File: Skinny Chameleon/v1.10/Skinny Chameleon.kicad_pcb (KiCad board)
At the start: 2 copper layers, 225.4 x 91.9 mm, 206 parts, among them SW10 PG151101S11, SW11 PG151101S11, SW13 PG151101S11, SW14 PG151101S11, SW15 PG151101S11, SW16 PG151101S11, SW17 PG151101S11, SW18 PG151101S11, SW19 PG151101S11, SW2 PG151101S11, SW20 PG151101S11, SW21 PG151101S11, SW22 PG151101S11, SW23 PG151101S11, SW24 PG151101S11, SW25 PG151101S11, SW26 PG151101S11, SW27 PG151101S11, SW28 PG151101S11, SW29 PG151101S11, SW3 PG151101S11, SW30 PG151101S11, SW31 PG151101S11, SW32 PG151101S11, SW33 PG151101S11, SW34 PG151101S11, SW35 PG151101S11, SW36 PG151101S11, SW38 PG151101S11, SW39 PG151101S11, SW4 PG151101S11, SW40 PG151101S11, SW41 PG151101S11, SW42 PG151101S11, SW43 PG151101S11, SW44 PG151101S11, SW45 PG151101S11, SW46 PG151101S11, SW47 PG151101S11, SW5 PG151101S11, SW50 PG151101S11, SW51 PG151101S11, SW52 PG151101S11, SW53 PG151101S11, SW54 PG151101S11, SW55 PG151101S11, SW56 PG151101S11, SW57 PG151101S11, SW58 PG151101S11, SW59 PG151101S11, SW6 PG151101S11, SW61 PG151101S11, SW62 PG151101S11, SW63 PG151101S11, SW64 PG151101S11, SW65 PG151101S11, SW66 PG151101S11, SW67 YTSA010, SW68 YTSA010, SW7 PG151101S11, SW8 PG151101S11, SW9 PG151101S11, U1 SPX3819M5-L-3-3/TR, U2 W25Q32JVUUIQ, U3 RP2040, U4 SN74LV1T34DBV, U5 SRV05-4, Y1 TXM12M0004252LBCEO00T

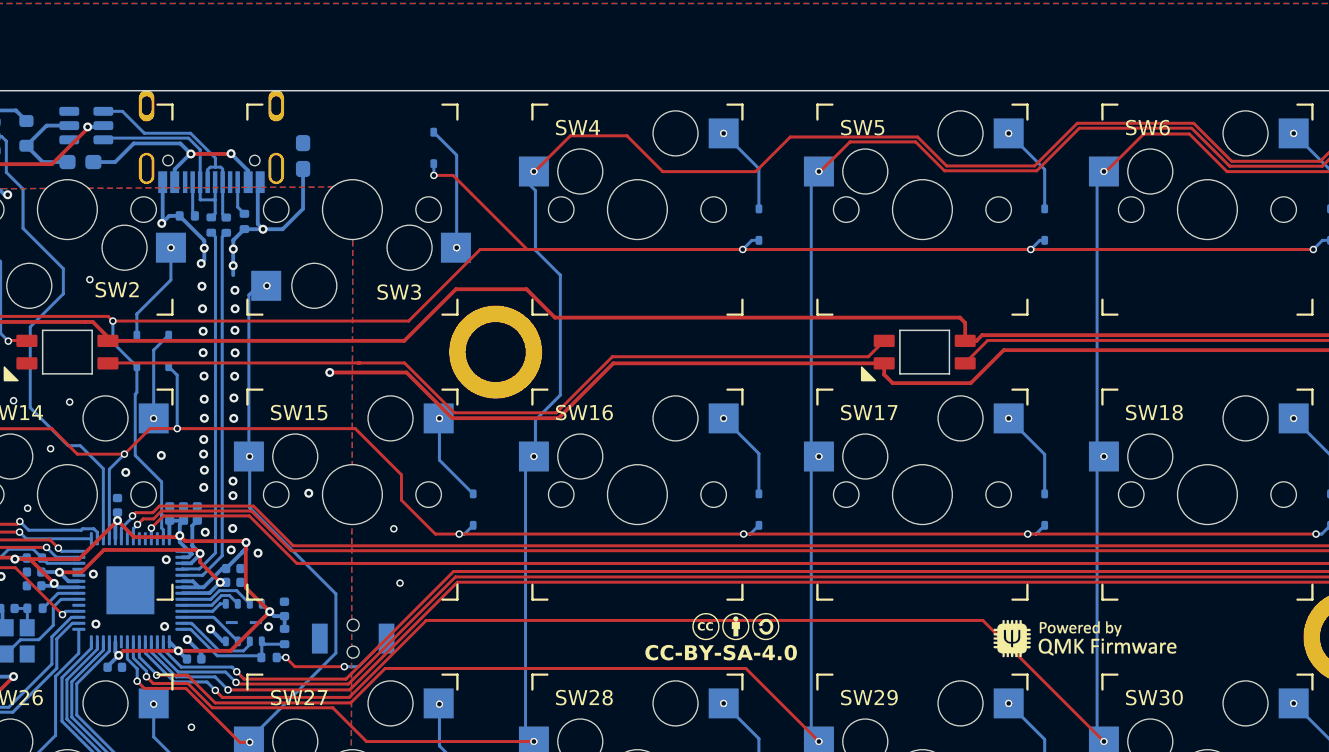
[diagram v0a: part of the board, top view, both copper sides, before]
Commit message: Skinny Chamelelon v1.10
- Updated Planck Mounting holes
- Updated centering on USB (was centered on 19.05 spacing?)
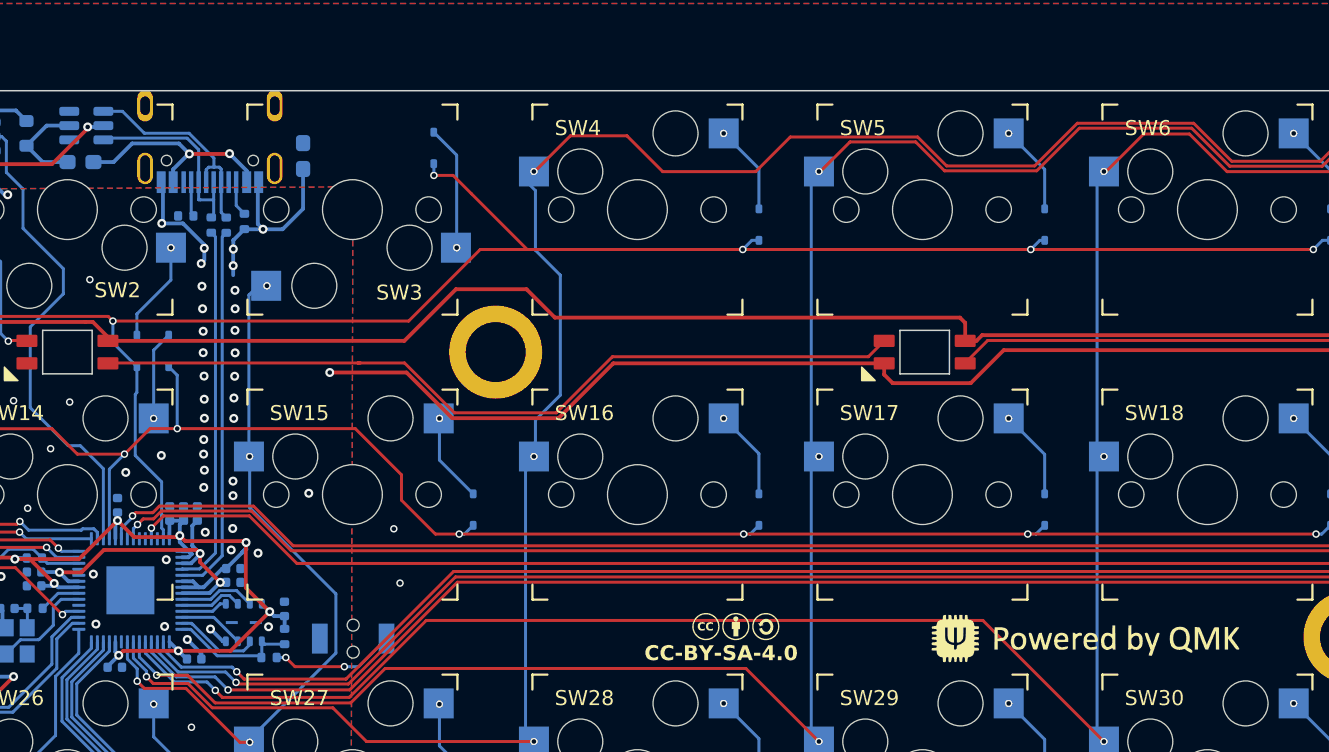
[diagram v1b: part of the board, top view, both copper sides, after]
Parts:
- Logo2: footprint Logotypes:Powered_by_QMK -> Logotypes:qmk logo
- USB1: footprint LCSC_Library:HRO_TYPE-C-31-M-12 -> Keyboard Common:HRO_TYPE-C-31-M-12
- moved R1 0.10 mm to (69.1, 54.5)
- moved USB1 0.10 mm to (70.7, 47.1)
